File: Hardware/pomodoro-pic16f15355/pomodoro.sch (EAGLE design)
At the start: 33 parts, among them IC1 PIC16F15355T-I_SO

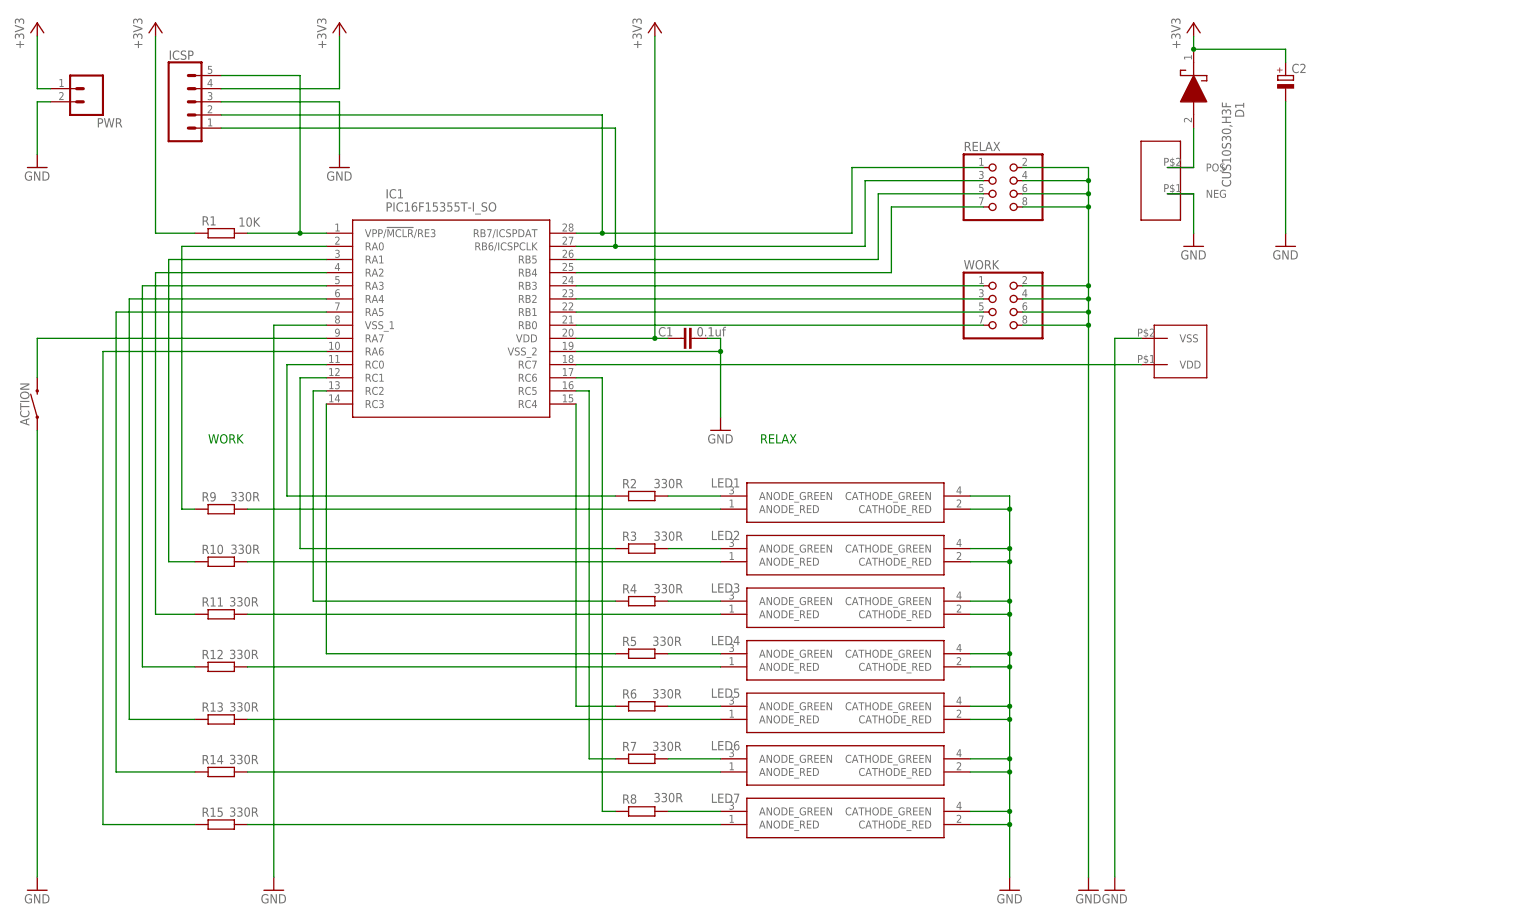
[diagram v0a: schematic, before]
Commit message: Switched out diode and added pchannel mosfet, rounded corners, generated new gergbers
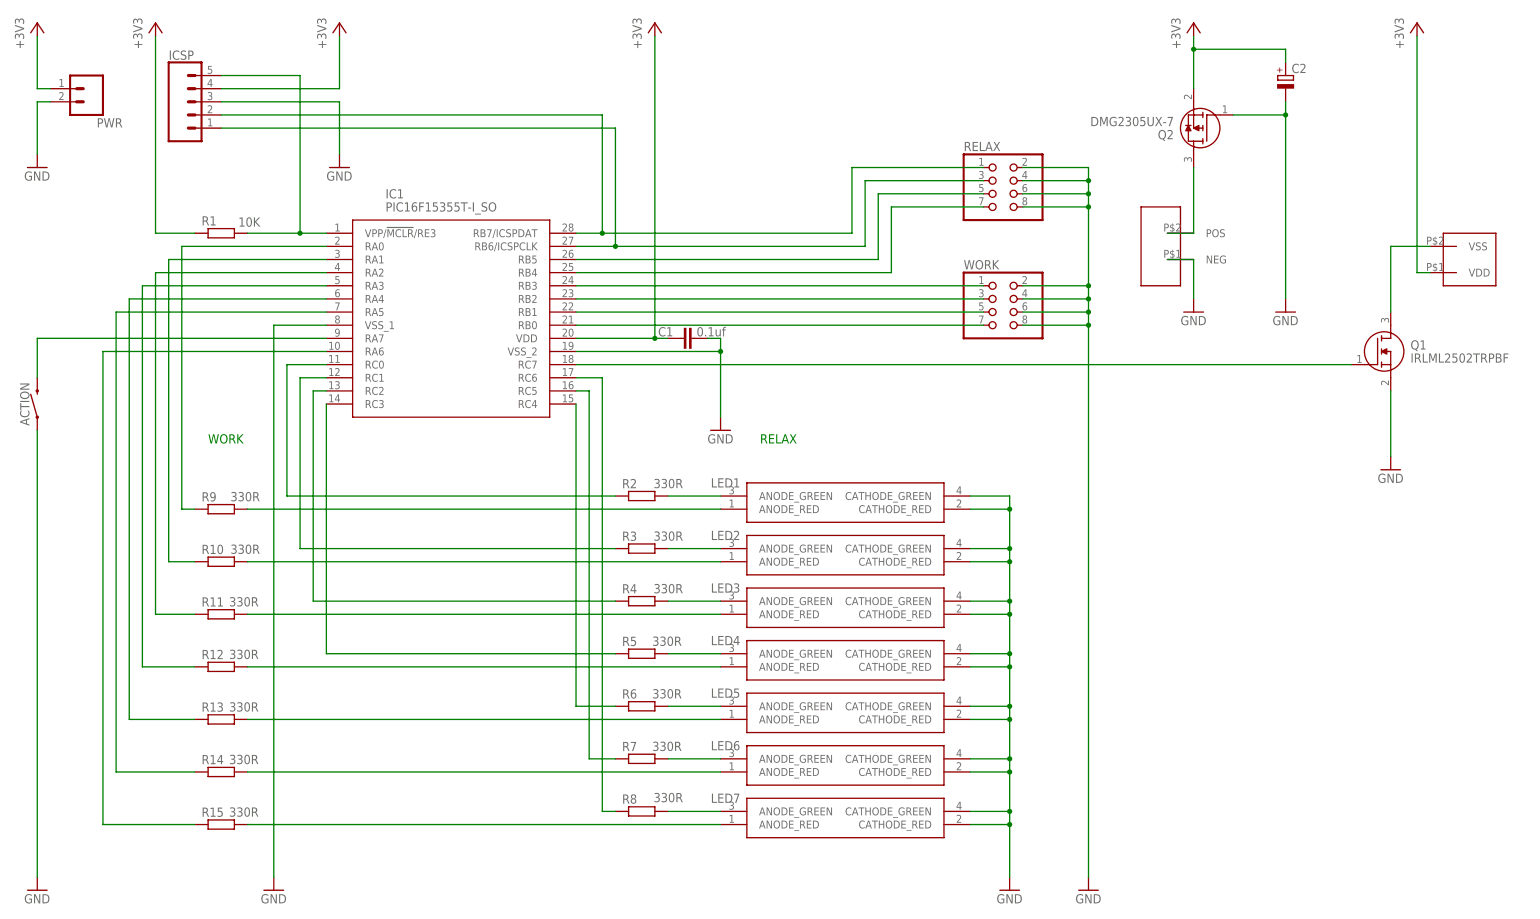
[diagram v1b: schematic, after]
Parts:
- removed D1: CUS10S30,H3F, CUS10S30_H3F:CUS10S30,H3F
- added Q1: IRLML2502TRPBF, IRLML2502TRPBF:IRLML2502TRPBF
- added Q2: DMG2305UX-7, DMG2305UX-7:DMG2305UX-7
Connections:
- new net N$40: Q1.D, U$2.VSS
- net +3V3: now also Q2.S, U$2.VDD; no longer D1.K
- net GND: now also Q1.S, Q2.G; no longer U$2.VSS
- net N$26: now also Q1.G; no longer U$2.VDD
- net N$41: now also Q2.D; no longer D1.A
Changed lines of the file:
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@@
 <part name="U$2" library="buzzer" deviceset="BUZZER8X8" device=""/>
 <part name="GND10" library="supply1" library_urn="urn:adsk.eagle:library:371" deviceset="GND" device=""/>
-<part name="D1" library="CUS10S30_H3F" deviceset="CUS10S30,H3F" device=""/>
 <part name="C2" library="rcl" library_urn="urn:adsk.eagle:library:334" deviceset="CPOL-EU" device="E2.5-5" package3d_urn="urn:adsk.eagle:package:23344/1"/>
 <part name="GND11" library="supply1" library_urn="urn:adsk.eagle:library:371" deviceset="GND" device=""/>
@@
 <part name="LED7" library="APBD3224LSURKCGKC" deviceset="APBD3224LSURKCGKC" device=""/>
 <part name="GND12" library="supply1" library_urn="urn:adsk.eagle:library:371" deviceset="GND" device=""/>
+<part name="Q1" library="IRLML2502TRPBF" deviceset="IRLML2502TRPBF" device=""/>
+<part name="+3V6" library="supply1" library_urn="urn:adsk.eagle:library:371" deviceset="+3V3" device=""/>
+<part name="Q2" library="DMG2305UX-7" deviceset="DMG2305UX-7" device=""/>
 </parts>
 <sheets>
@@
 <attribute name="VALUE" x="86.36" y="20.32" size="1.778" layer="96"/>
 </instance>
-<instance part="GND4" gate="1" x="165.1" y="-66.04" smashed="yes">
-<attribute name="VALUE" x="162.56" y="-68.58" size="1.778" layer="96"/>
+<instance part="GND4" gate="1" x="218.44" y="15.24" smashed="yes">
+<attribute name="VALUE" x="215.9" y="12.7" size="1.778" layer="96"/>
 </instance>
 <instance part="PWR" gate="G$1" x="-33.02" y="88.9" smashed="yes" rot="R180">
@@
 <attribute name="NAME" x="-44.704" y="27.94" size="1.778" layer="95" font="vector" rot="R90" align="bottom-center"/>
 </instance>
-<instance part="U$1" gate="G$1" x="190.5" y="60.96" smashed="yes"/>
+<instance part="U$1" gate="G$1" x="190.5" y="48.26" smashed="yes"/>
 <instance part="+3V5" gate="G$1" x="180.34" y="101.6" smashed="yes">
 <attribute name="VALUE" x="177.8" y="96.52" size="1.778" layer="96" rot="R90"/>
@@
 <attribute name="NAME" x="-17.78" y="94.488" size="1.778" layer="95" font="vector"/>
 </instance>
-<instance part="U$2" gate="G$1" x="177.8" y="38.1" smashed="yes" rot="R180"/>
-<instance part="GND10" gate="1" x="180.34" y="58.42" smashed="yes">
-<attribute name="VALUE" x="177.8" y="55.88" size="1.778" layer="96"/>
-</instance>
-<instance part="D1" gate="G$1" x="180.34" y="99.06" smashed="yes" rot="R270">
-<attribute name="NAME" x="189.23" y="86.36" size="1.778" layer="95" rot="R270" align="center-left"/>
-<attribute name="VALUE" x="186.69" y="86.36" size="1.778" layer="96" rot="R270" align="center-left"/>
+<instance part="U$2" gate="G$1" x="233.68" y="55.88" smashed="yes" rot="R180"/>
+<instance part="GND10" gate="1" x="180.34" y="45.72" smashed="yes">
+<attribute name="VALUE" x="177.8" y="43.18" size="1.778" layer="96"/>
 </instance>
 <instance part="C2" gate="G$1" x="198.12" y="91.44" smashed="yes">
@@
 <attribute name="VALUE" x="199.263" y="86.8426" size="1.778" layer="96"/>
 </instance>
-<instance part="GND11" gate="1" x="198.12" y="58.42" smashed="yes">
-<attribute name="VALUE" x="195.58" y="55.88" size="1.778" layer="96"/>
+<instance part="GND11" gate="1" x="198.12" y="45.72" smashed="yes">
+<attribute name="VALUE" x="195.58" y="43.18" size="1.778" layer="96"/>
 </instance>
 <instance part="LED1" gate="G$1" x="137.16" y="7.62" smashed="yes" rot="R180">
@@
 <instance part="GND12" gate="1" x="144.78" y="-66.04" smashed="yes">
 <attribute name="VALUE" x="142.24" y="-68.58" size="1.778" layer="96"/>
+</instance>
+<instance part="Q1" gate="G$1" x="210.82" y="35.56" smashed="yes">
+<attribute name="NAME" x="222.25" y="39.37" size="1.778" layer="95" align="center-left"/>
+<attribute name="VALUE" x="222.25" y="36.83" size="1.778" layer="96" align="center-left"/>
+</instance>
+<instance part="+3V6" gate="G$1" x="223.52" y="101.6" smashed="yes">
+<attribute name="VALUE" x="220.98" y="96.52" size="1.778" layer="96" rot="R90"/>
+</instance>
+<instance part="Q2" gate="G$1" x="187.96" y="83.82" smashed="yes" rot="R180">
+<attribute name="NAME" x="176.53" y="80.01" size="1.778" layer="95" rot="R180" align="center-left"/>
+<attribute name="VALUE" x="176.53" y="82.55" size="1.778" layer="96" rot="R180" align="center-left"/>
 </instance>
 </instances>
@@
 </segment>
 <segment>
-<pinref part="D1" gate="G$1" pin="K"/>
-<pinref part="+3V5" gate="G$1" pin="+3V3"/>
-<wire x1="180.34" y1="96.52" x2="180.34" y2="99.06" width="0.1524" layer="91"/>
+<pinref part="U$2" gate="G$1" pin="VDD"/>
+<wire x1="226.06" y1="53.34" x2="223.52" y2="53.34" width="0.1524" layer="91"/>
+<wire x1="223.52" y1="53.34" x2="223.52" y2="99.06" width="0.1524" layer="91"/>
+<pinref part="+3V6" gate="G$1" pin="+3V3"/>
+</segment>
+<segment>
 <pinref part="C2" gate="G$1" pin="+"/>
 <wire x1="180.34" y1="96.52" x2="198.12" y2="96.52" width="0.1524" layer="91"/>
 <wire x1="198.12" y1="96.52" x2="198.12" y2="93.98" width="0.1524" layer="91"/>
+<pinref part="+3V5" gate="G$1" pin="+3V3"/>
+<wire x1="180.34" y1="99.06" x2="180.34" y2="96.52" width="0.1524" layer="91"/>
+<pinref part="Q2" gate="G$1" pin="S"/>
+<wire x1="180.34" y1="96.52" x2="180.34" y2="88.9" width="0.1524" layer="91"/>
 <junction x="180.34" y="96.52"/>
 </segment>
@@
 </segment>
 <segment>
-<wire x1="165.1" y1="40.64" x2="165.1" y2="-63.5" width="0.1524" layer="91"/>
-<pinref part="GND4" gate="1" pin="GND"/>
-<pinref part="U$2" gate="G$1" pin="VSS"/>
-<wire x1="165.1" y1="40.64" x2="170.18" y2="40.64" width="0.1524" layer="91"/>
-</segment>
-<segment>
 <pinref part="PWR" gate="G$1" pin="2"/>
 <wire x1="-40.64" y1="86.36" x2="-43.18" y2="86.36" width="0.1524" layer="91"/>
@@
 <pinref part="U$1" gate="G$1" pin="NEG"/>
 <pinref part="GND10" gate="1" pin="GND"/>
-<wire x1="175.26" y1="68.58" x2="180.34" y2="68.58" width="0.1524" layer="91"/>
-<wire x1="180.34" y1="68.58" x2="180.34" y2="60.96" width="0.1524" layer="91"/>
+<wire x1="175.26" y1="55.88" x2="180.34" y2="55.88" width="0.1524" layer="91"/>
+<wire x1="180.34" y1="55.88" x2="180.34" y2="48.26" width="0.1524" layer="91"/>
 </segment>
 <segment>
 <pinref part="C2" gate="G$1" pin="-"/>
-<wire x1="198.12" y1="86.36" x2="198.12" y2="60.96" width="0.1524" layer="91"/>
+<wire x1="198.12" y1="86.36" x2="198.12" y2="83.82" width="0.1524" layer="91"/>
 <pinref part="GND11" gate="1" pin="GND"/>
+<pinref part="Q2" gate="G$1" pin="G"/>
+<wire x1="198.12" y1="83.82" x2="198.12" y2="48.26" width="0.1524" layer="91"/>
+<wire x1="187.96" y1="83.82" x2="198.12" y2="83.82" width="0.1524" layer="91"/>
+<junction x="198.12" y="83.82"/>
 </segment>
 <segment>
@@
 <pinref part="GND12" gate="1" pin="GND"/>
 </segment>
+<segment>
+<pinref part="GND4" gate="1" pin="GND"/>
+<pinref part="Q1" gate="G$1" pin="S"/>
+<wire x1="218.44" y1="17.78" x2="218.44" y2="30.48" width="0.1524" layer="91"/>
+</segment>
 </net>
 <net name="N$4" class="0">
@@
 </segment>
 </net>
-<net name="N$26" class="0">
-<segment>
-<pinref part="IC1" gate="G$1" pin="RC7"/>
-<pinref part="U$2" gate="G$1" pin="VDD"/>
-<wire x1="60.96" y1="35.56" x2="170.18" y2="35.56" width="0.1524" layer="91"/>
-</segment>
-</net>
 <net name="N$41" class="0">
 <segment>
 <pinref part="U$1" gate="G$1" pin="POS"/>
-<pinref part="D1" gate="G$1" pin="A"/>
-<wire x1="175.26" y1="73.66" x2="180.34" y2="73.66" width="0.1524" layer="91"/>
-<wire x1="180.34" y1="73.66" x2="180.34" y2="81.28" width="0.1524" layer="91"/>
+<wire x1="175.26" y1="60.96" x2="180.34" y2="60.96" width="0.1524" layer="91"/>
+<wire x1="180.34" y1="60.96" x2="180.34" y2="73.66" width="0.1524" layer="91"/>
+<pinref part="Q2" gate="G$1" pin="D"/>
 </segment>
 </net>
@@
 </segment>
 </net>
+<net name="N$26" class="0">
+<segment>
+<pinref part="IC1" gate="G$1" pin="RC7"/>
+<pinref part="Q1" gate="G$1" pin="G"/>
+<wire x1="60.96" y1="35.56" x2="210.82" y2="35.56" width="0.1524" layer="91"/>
+</segment>
+</net>
+<net name="N$40" class="0">
+<segment>
+<pinref part="Q1" gate="G$1" pin="D"/>
+<wire x1="218.44" y1="45.72" x2="218.44" y2="58.42" width="0.1524" layer="91"/>
+<pinref part="U$2" gate="G$1" pin="VSS"/>
+<wire x1="218.44" y1="58.42" x2="226.06" y2="58.42" width="0.1524" layer="91"/>
+</segment>
+</net>
